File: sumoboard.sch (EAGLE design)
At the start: 23 parts

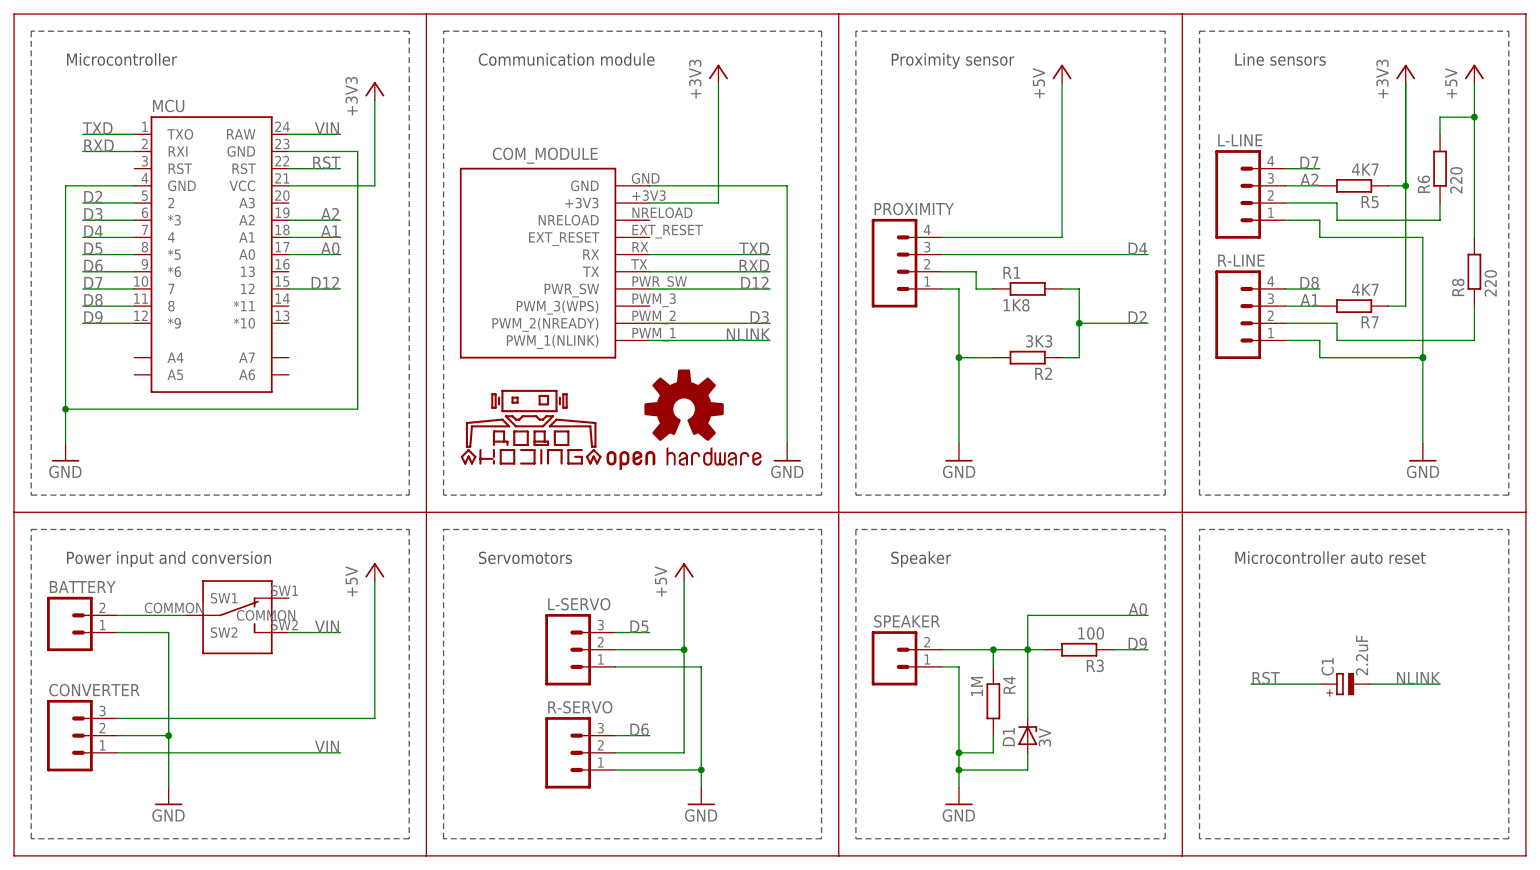
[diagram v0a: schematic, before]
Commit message: updated sumoboard
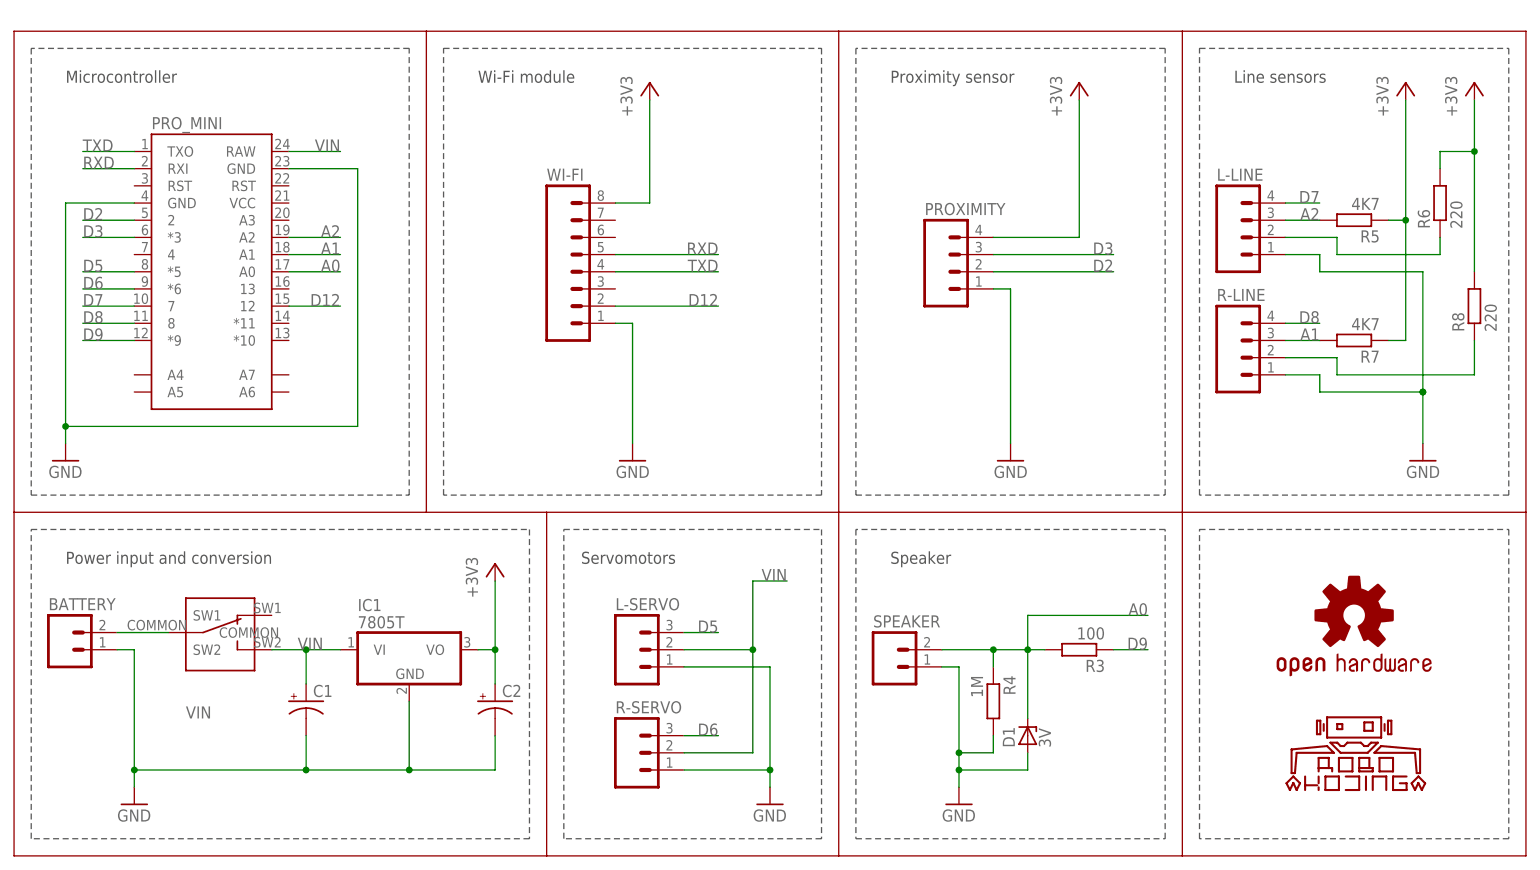
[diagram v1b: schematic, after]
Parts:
- removed COM_MODULE: USR_WIFI-T, usr_wifi:USR_WIFI-T
- removed CONVERTER: (no value), SparkFun-Connectors:M03LOCK_LONGPADS
- removed MCU: ARDUINO_PRO_MINI, SparkFun-Boards:ARDUINO_PRO_MINI
- removed R1: 1K8, Child-Friendly-Parts:R-EU_0204/5
- removed R2: 3K3, Child-Friendly-Parts:R-EU_0204/5
- added C2: (no value), rcl:CPOL-USE5-10.5
- added IC1: 7805T, linear:7805T
- added PRO_MINI: ARDUINO_PRO_MINI, SparkFun-Boards:ARDUINO_PRO_MINI
- added WI-FI: (no value), SparkFun-Connectors:M08LOCK_LONGPADS
- C1: value 2.2uF -> (none); device Child-Friendly-Parts:CPOL-EUE2-5 -> rcl:CPOL-USE5-10.5
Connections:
- removed net +5V: CONVERTER.3, L-SERVO.2, PROXIMITY.4, R-SERVO.2, R6.2, R8.2
- removed net D4: MCU.4, PROXIMITY.3
- removed net N$1: PROXIMITY.2, R1.1
- removed net NLINK: C1.-, COM_MODULE.PWM_1(NLINK)
- removed net RST: C1.+, MCU.RST@2
- net +3V3: now also C2.+, IC1.VO, PROXIMITY.4, R6.2, R8.2, WI-FI.8; no longer COM_MODULE.+3V3, MCU.VCC
- net A0: now also PRO_MINI.A0; no longer MCU.A0
- net A1: now also PRO_MINI.A1; no longer MCU.A1
- net A2: now also PRO_MINI.A2; no longer MCU.A2
- net D12: now also PRO_MINI.12, WI-FI.2; no longer COM_MODULE.PWR_SW, MCU.12
- net D2: now also PROXIMITY.2, PRO_MINI.2; no longer MCU.2, R1.2, R2.1
- net D3: now also PROXIMITY.3, PRO_MINI.*3; no longer COM_MODULE.PWM_2(NREADY), MCU.*3
- net D5: now also PRO_MINI.*5; no longer MCU.*5
- net D6: now also PRO_MINI.*6; no longer MCU.*6
- net D7: now also PRO_MINI.7; no longer MCU.7
- net D8: now also PRO_MINI.8; no longer MCU.8
- net D9: now also PRO_MINI.*9; no longer MCU.*9
- net GND: now also C1.-, C2.-, IC1.GND, PRO_MINI.GND, PRO_MINI.GND@2, WI-FI.1; no longer COM_MODULE.GND, CONVERTER.2, MCU.GND, MCU.GND@2, R2.2
- net RXD: now also PRO_MINI.RXI, WI-FI.5; no longer COM_MODULE.TX, MCU.RXI
- net TXD: now also PRO_MINI.TXO, WI-FI.4; no longer COM_MODULE.RX, MCU.TXO
- net VIN: now also C1.+, IC1.VI, L-SERVO.2, PRO_MINI.RAW, R-SERVO.2; no longer CONVERTER.1, MCU.RAW
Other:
- note added: "Wi-Fi module"
- note removed: "Communication module"
- note removed: "Microcontroller auto reset"
- moved on the sheet: BATTERY, C1, L-LINE, L-SERVO, PROXIMITY, R-LINE, R-SERVO, R5, R6, R7, R8
